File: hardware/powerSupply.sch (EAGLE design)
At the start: 92 parts, among them IC1 MCP3008, IC2 LM334Z, IC3 MCP4821P, IC4 MCP4821P, IC5 74LS139D, IC6 7805TV, IC7 LP2950Z, J1 1X2-3.5MM, J2 1X2-3.5MM, J4 RASPBERRYPI-40-PIN-GPIO_PTH, SW1 EC11B_SW, SW2 EC11B_SW, T1 2N3904, T2 2N3904, U1 LM358, U2 LM358, U3 MAX874CPA, U4 LM358

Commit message: 
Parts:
- removed TM1: (no value), adafruit:TRIMPOTTC33X
- added J3: RASPBERRYPI-40-PIN-GPIO_PTH, Hexellence-Connectors:RASPBERRYPI-40-PIN-GPIO_PTH
- added R40, R41: 10K, rcl:R-US_0204/7
- C11, C18, C19, C20, C6: value 2.2u -> 2u2; device rcl:CPOL-USE5-6 -> adafruit:CPOL-USE2-5
- C3: value 2.2u -> 100n; device rcl:CPOL-USE5-6 -> adafruit:C-US050-024X044
- C5: value 100n -> 2u2; device adafruit:C-US050-024X044 -> adafruit:CPOL-USE2-5
- J4: value RASPBERRYPI-40-PIN-GPIO_PTH -> 1X2-3.5MM; device Hexellence-Connectors:RASPBERRYPI-40-PIN-GPIO_PTH -> adafruit:1X2-3.5MM
- renumbered U$1 to IC8, U1 to IC13, U2 to IC12, U3 to IC9, U4 to ICG3, U5 to IC11
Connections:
- net 0.064@25C renamed 0.064V@25C
- net 5V: now also C19.+, R41.2; no longer C18.+, TM1.A
- net A0: now also J3.GP6; no longer J4.GP6
- net A1: now also J3.GP5; no longer J4.GP5
- net ADC_IOUT: now also IC1.CH3
- net GND: now also C3.2, C5.-, J3.GND@14, J3.GND@20, J3.GND@25, J3.GND@30, J3.GND@34, J3.GND@39, J3.GND@6, J3.GND@9, J4.2; no longer C3.-, C5.2, J4.GND@14, J4.GND@20, J4.GND@25, J4.GND@30, J4.GND@34, J4.GND@39, J4.GND@6, J4.GND@9
- net MISO: now also J3.MISO; no longer J4.MISO
- net MOSI: now also J3.MOSI; no longer J4.MOSI
- net N$10: now also C4.1; no longer C5.1
- net N$18: now also R40.2; no longer TM1.E
- net N$21: now also J3.GP4; no longer J4.GP4
- net N$23: now also J3.GP19; no longer J4.GP19
- net N$24: now also J3.GP16; no longer J4.GP16
- net N$26: now also J3.GP20; no longer J4.GP20
- net N$27: now also J3.GP21; no longer J4.GP21
- net N$3: now also R40.1, R41.1; no longer TM1.S
- net N$30: now also J3.GP23; no longer J4.GP23
- net N$31: now also J3.GP24; no longer J4.GP24
- net N$32: now also J3.GP25; no longer J4.GP25
- net N$33: now also J3.GP26; no longer J4.GP26
- net N$34: now also J3.SDA; no longer J4.SDA
- net N$35: now also J3.SCL; no longer J4.SCL
- net OE0: now also J3.CE0; no longer J4.CE0
- net OE1: now also J3.CE1; no longer J4.CE1
- net SCLK: now also J3.SCLK; no longer J4.SCLK
- net V+: now also C18.+, J4.1; no longer C19.+
- net V+1: now also C3.1; no longer C4.1
- net VADJ: now also C5.+; no longer C3.+
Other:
- note added: "Comparator"
- note added: "Differential amplifier, Vo = Rf/Rg(Vp-Vn), Vo = Vp-Vn"
- note added: "Non inverting amplifier Gain: 10"
- note added: "Vref: 2048mV"
- moved on the sheet: C18, C19, C4

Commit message: 
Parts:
- removed J1, J2, J4: 1X2-3.5MM, adafruit:1X2-3.5MM
- added J5, J6, J7: (no value), Hexellence-Connectors:CONN_022.54MM_SCREWTERM
- C14, C15, C16, C17: value 100n -> 10n
- R10, R11, R2, R3, R4, R5, R6, R7, R8, R9: device rcl:R-US_0204/7 -> adafruit:R-US_0207/12
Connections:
- net GND: now also J5.2, J6.2, J7.2; no longer J1.2, J2.2, J4.2
- net V+: now also J5.1; no longer J4.1
- net VOUT: now also J6.1; no longer J1.1
- net VSENS: now also J7.1; no longer J2.1

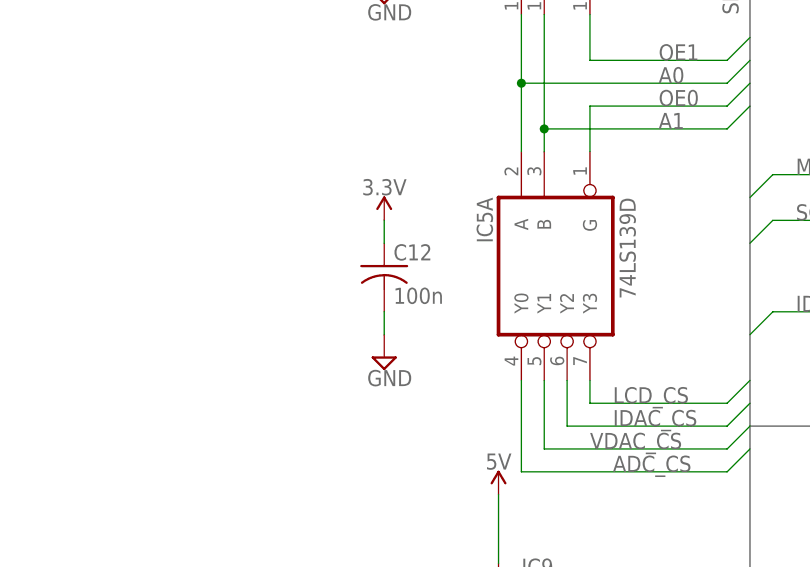
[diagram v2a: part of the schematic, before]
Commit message: 
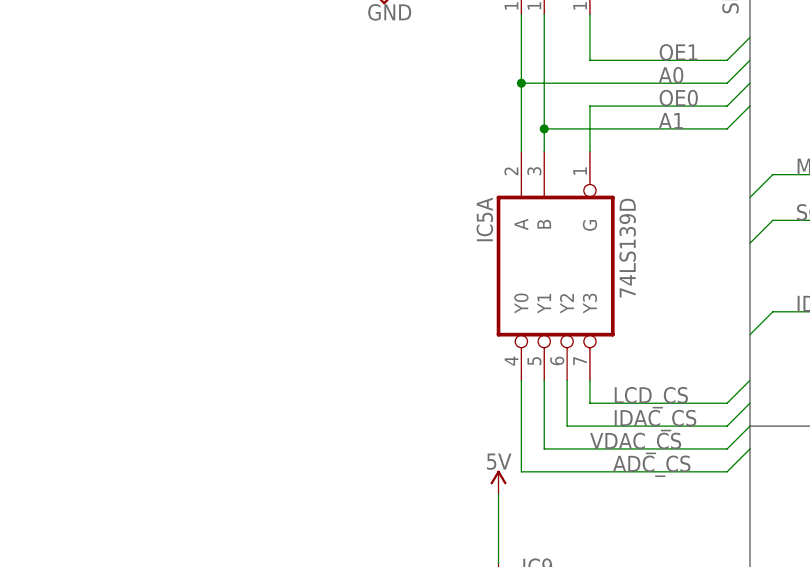
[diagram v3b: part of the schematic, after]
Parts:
- removed C12: 100n, adafruit:C-US050-024X044
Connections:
- net 3.3V: no longer C12.1
- net GND: no longer C12.2
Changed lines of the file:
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@@
 <part name="IC5" library="74xx-us" library_urn="urn:adsk.eagle:library:88" deviceset="74*139" device="D" package3d_urn="urn:adsk.eagle:package:2918/1" technology="LS"/>
 <part name="C10" library="adafruit" library_urn="urn:adsk.eagle:library:420" deviceset="C-US" device="050-024X044" package3d_urn="urn:adsk.eagle:package:6240356/1" value="100n"/>
-<part name="C12" library="adafruit" library_urn="urn:adsk.eagle:library:420" deviceset="C-US" device="050-024X044" package3d_urn="urn:adsk.eagle:package:6240356/1" value="100n"/>
 <part name="SUPPLY27" library="supply2" library_urn="urn:adsk.eagle:library:372" deviceset="GND" device=""/>
-<part name="SUPPLY28" library="supply2" library_urn="urn:adsk.eagle:library:372" deviceset="GND" device=""/>
 <part name="SUPPLY29" library="SparkFun-PowerSymbols" deviceset="3.3V" device=""/>
-<part name="SUPPLY30" library="SparkFun-PowerSymbols" deviceset="3.3V" device=""/>
 <part name="SUPPLY31" library="SparkFun-PowerSymbols" deviceset="3.3V" device=""/>
 <part name="LCD1" library="Hexellence-Displays" deviceset="LCD-16X2" device="SILK"/>
@@
 <attribute name="VALUE" x="13.716" y="72.009" size="1.778" layer="96"/>
 </instance>
-<instance part="C12" gate="G$1" x="12.7" y="35.56" smashed="yes" grouprefs="SPI_CS_EXT">
-<attribute name="NAME" x="13.716" y="36.195" size="1.778" layer="95"/>
-<attribute name="VALUE" x="13.716" y="31.369" size="1.778" layer="96"/>
-</instance>
 <instance part="SUPPLY27" gate="GND" x="12.7" y="66.04" smashed="yes" grouprefs="SPI_CS_EXT">
 <attribute name="VALUE" x="10.795" y="62.865" size="1.778" layer="96"/>
 </instance>
-<instance part="SUPPLY28" gate="GND" x="12.7" y="25.4" smashed="yes" grouprefs="SPI_CS_EXT">
-<attribute name="VALUE" x="10.795" y="22.225" size="1.778" layer="96"/>
-</instance>
 <instance part="SUPPLY29" gate="G$1" x="12.7" y="81.28" smashed="yes" grouprefs="SPI_CS_EXT">
 <attribute name="VALUE" x="12.7" y="84.074" size="1.778" layer="96" align="bottom-center"/>
-</instance>
-<instance part="SUPPLY30" gate="G$1" x="12.7" y="40.64" smashed="yes" grouprefs="SPI_CS_EXT">
-<attribute name="VALUE" x="12.7" y="43.434" size="1.778" layer="96" align="bottom-center"/>
 </instance>
 <instance part="SUPPLY31" gate="G$1" x="99.06" y="101.6" smashed="yes">
@@
 <pinref part="C10" gate="G$1" pin="2"/>
 <wire x1="12.7" y1="68.58" x2="12.7" y2="71.12" width="0.1524" layer="91" grouprefs="SPI_CS_EXT"/>
-</segment>
-<segment>
-<pinref part="SUPPLY28" gate="GND" pin="GND"/>
-<pinref part="C12" gate="G$1" pin="2"/>
-<wire x1="12.7" y1="27.94" x2="12.7" y2="30.48" width="0.1524" layer="91" grouprefs="SPI_CS_EXT"/>
 </segment>
 <segment>
@@
 </segment>
 <segment>
-<pinref part="C12" gate="G$1" pin="1"/>
-<pinref part="SUPPLY30" gate="G$1" pin="3.3V"/>
-<wire x1="12.7" y1="38.1" x2="12.7" y2="40.64" width="0.1524" layer="91" grouprefs="SPI_CS_EXT"/>
-</segment>
-<segment>

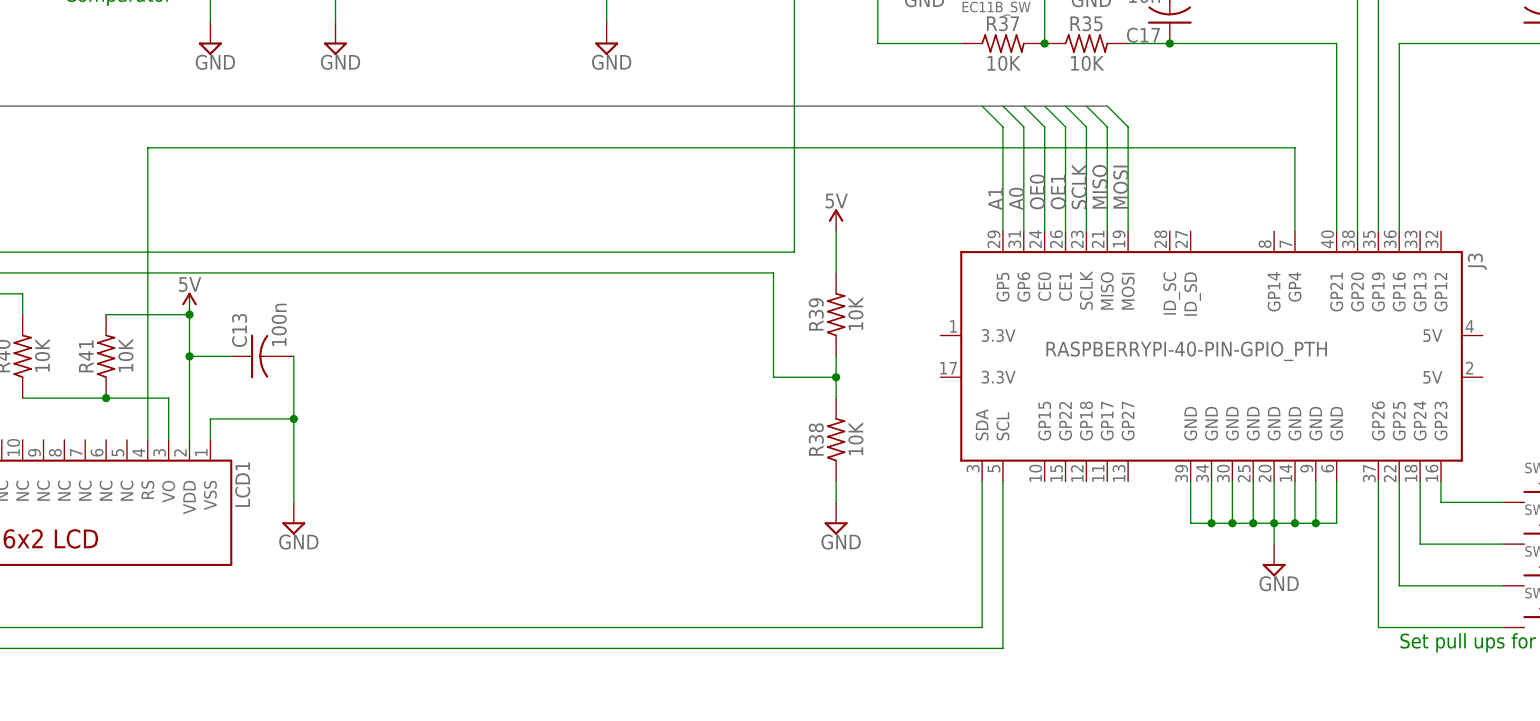
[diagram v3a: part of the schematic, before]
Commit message: 
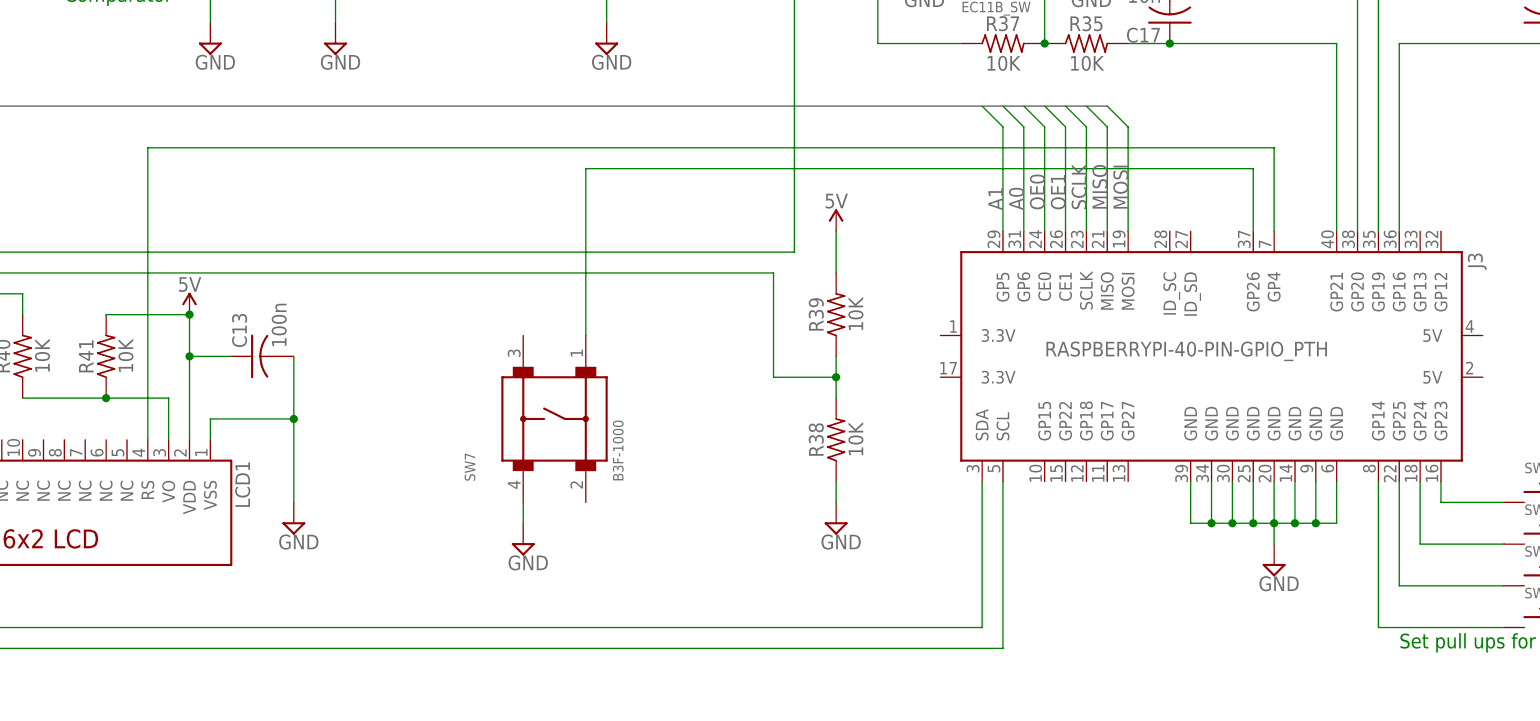
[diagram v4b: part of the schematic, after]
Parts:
- added SW7: B3F-1000, Switch:B3F-1000
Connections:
- new net N$36: J3.GP26, SW7.1
- net N$33: now also J3.GP14; no longer J3.GP26
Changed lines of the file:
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@@
 <layer number="132" name="bAdjust" color="7" fill="1" visible="yes" active="yes"/>
 <layer number="144" name="Drill_legend" color="7" fill="1" visible="yes" active="yes"/>
+<layer number="145" name="DrillLegend_01-16" color="2" fill="9" visible="no" active="yes"/>
+<layer number="146" name="DrillLegend_01-20" color="3" fill="9" visible="no" active="yes"/>
 <layer number="150" name="Notes" color="7" fill="1" visible="yes" active="yes"/>
 <layer number="151" name="HeatSink" color="7" fill="1" visible="yes" active="yes"/>
@@
 <part name="J6" library="Hexellence-Connectors" deviceset="CONN_02" device="2.54MM_SCREWTERM" package3d_urn="urn:adsk.eagle:package:38059/1"/>
 <part name="J7" library="Hexellence-Connectors" deviceset="CONN_02" device="2.54MM_SCREWTERM" package3d_urn="urn:adsk.eagle:package:38059/1"/>
+<part name="SW7" library="Switch" library_urn="urn:adsk.eagle:library:11396471" deviceset="B3F-1000" device="" package3d_urn="urn:adsk.eagle:package:10899221/2"/>
+<part name="SUPPLY28" library="supply2" library_urn="urn:adsk.eagle:library:372" deviceset="GND" device=""/>
 </parts>
 <sheets>
@@
 <attribute name="VALUE" x="340.36" y="111.506" size="1.778" layer="96" font="vector" rot="R180"/>
 <attribute name="NAME" x="340.36" y="101.092" size="1.778" layer="95" font="vector" rot="R180"/>
+</instance>
+<instance part="SW7" gate="G$1" x="200.66" y="-20.32" smashed="yes" rot="R90">
+<attribute name="NAME" x="192.271890625" y="-27.946109375" size="1.27101875" layer="95" rot="R90"/>
+<attribute name="VALUE" x="210.32551875" y="-27.951590625" size="1.27193125" layer="96" rot="R90"/>
+</instance>
+<instance part="SUPPLY28" gate="GND" x="198.12" y="-35.56" smashed="yes">
+<attribute name="VALUE" x="196.215" y="-38.735" size="1.778" layer="96"/>
 </instance>
 </instances>
@@
 <wire x1="-12.7" y1="175.26" x2="-12.7" y2="180.34" width="0.1524" layer="91"/>
 <pinref part="J5" gate="G$1" pin="2"/>
+</segment>
+<segment>
+<pinref part="SUPPLY28" gate="GND" pin="GND"/>
+<wire x1="198.12" y1="-33.02" x2="198.12" y2="-30.48" width="0.1524" layer="91"/>
 </segment>
 </net>
@@
 <pinref part="LCD1" gate="LCD1" pin="RS"/>
 <wire x1="152.4" y1="-22.86" x2="152.4" y2="12.7" width="0.1524" layer="91"/>
-<wire x1="152.4" y1="12.7" x2="292.1" y2="12.7" width="0.1524" layer="91"/>
+<wire x1="152.4" y1="12.7" x2="289.56" y2="12.7" width="0.1524" layer="91"/>
 <pinref part="J3" gate="G$1" pin="GP4"/>
-<wire x1="292.1" y1="2.54" x2="292.1" y2="12.7" width="0.1524" layer="91"/>
+<wire x1="289.56" y1="2.54" x2="289.56" y2="12.7" width="0.1524" layer="91"/>
 </segment>
 </net>
@@
 <pinref part="SW6" gate="G$1" pin="P$1"/>
 <wire x1="317.5" y1="-45.72" x2="302.26" y2="-45.72" width="0.1524" layer="91"/>
-<pinref part="J3" gate="G$1" pin="GP26"/>
-<wire x1="302.26" y1="-45.72" x2="302.26" y2="-27.94" width="0.1524" layer="91"/>
+<pinref part="J3" gate="G$1" pin="GP14"/>
+<wire x1="302.26" y1="-27.94" x2="302.26" y2="-45.72" width="0.1524" layer="91"/>
 </segment>
 </net>
@@
 </segment>
 </net>
+<net name="N$36" class="0">
+<segment>
+<pinref part="SW7" gate="G$1" pin="1"/>
+<wire x1="205.74" y1="-10.16" x2="205.74" y2="10.16" width="0.1524" layer="91"/>
+<wire x1="205.74" y1="10.16" x2="287.02" y2="10.16" width="0.1524" layer="91"/>
+<pinref part="J3" gate="G$1" pin="GP26"/>
+<wire x1="287.02" y1="10.16" x2="287.02" y2="2.54" width="0.1524" layer="91"/>
+</segment>
+</net>

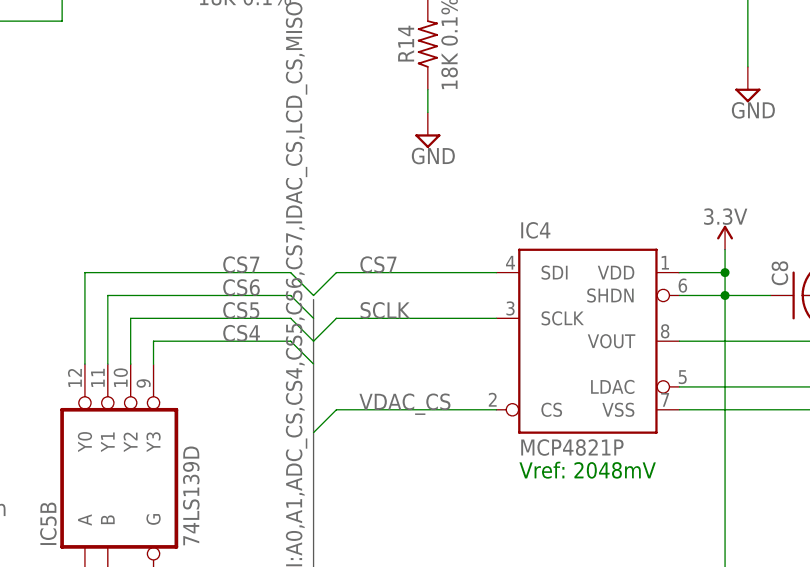
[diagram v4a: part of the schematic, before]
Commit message: 
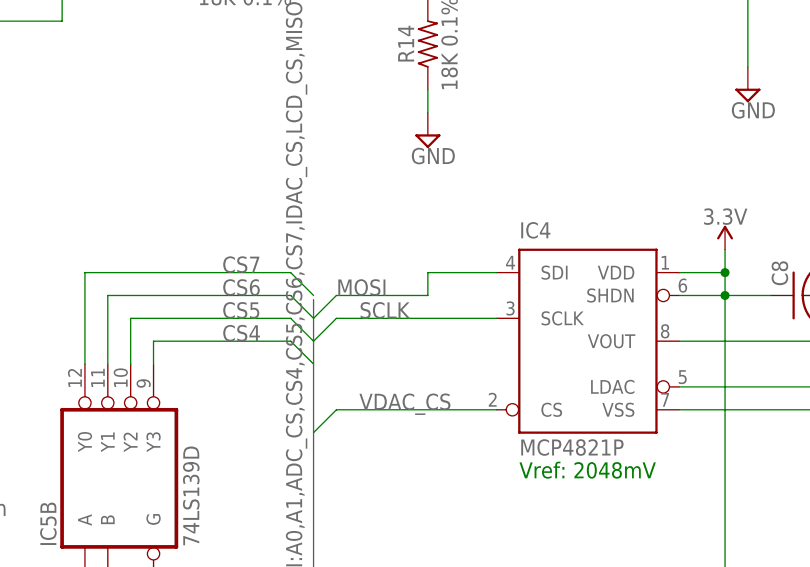
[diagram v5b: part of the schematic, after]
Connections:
- net CS7: no longer IC4.SDI
- net GND: now also SW7.4
- net MOSI: now also IC4.SDI
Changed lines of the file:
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@@
 <pinref part="SUPPLY28" gate="GND" pin="GND"/>
 <wire x1="198.12" y1="-33.02" x2="198.12" y2="-30.48" width="0.1524" layer="91"/>
+<pinref part="SW7" gate="G$1" pin="4"/>
 </segment>
 </net>
@@
 <pinref part="J3" gate="G$1" pin="MOSI"/>
 <wire x1="271.78" y1="2.54" x2="271.78" y2="15.24" width="0.1524" layer="91"/>
+</segment>
+<segment>
+<wire x1="53.34" y1="93.98" x2="55.88" y2="96.52" width="0.1524" layer="91"/>
+<label x="55.88" y="96.52" size="1.778" layer="95"/>
+<wire x1="55.88" y1="96.52" x2="66.04" y2="96.52" width="0.1524" layer="91"/>
+<wire x1="66.04" y1="96.52" x2="66.04" y2="99.06" width="0.1524" layer="91"/>
+<pinref part="IC4" gate="G$1" pin="SDI"/>
+<wire x1="66.04" y1="99.06" x2="73.66" y2="99.06" width="0.1524" layer="91"/>
 </segment>
 </net>
@@
 <pinref part="IC5" gate="B" pin="Y0"/>
 <wire x1="27.94" y1="99.06" x2="27.94" y2="88.9" width="0.1524" layer="91"/>
-<wire x1="53.34" y1="96.52" x2="55.88" y2="99.06" width="0.1524" layer="91"/>
-<wire x1="55.88" y1="99.06" x2="73.66" y2="99.06" width="0.1524" layer="91"/>
-<label x="58.42" y="99.06" size="1.778" layer="95"/>
-<pinref part="IC4" gate="G$1" pin="SDI"/>
-</segment>
-</net>
+</segment>
+</net>
